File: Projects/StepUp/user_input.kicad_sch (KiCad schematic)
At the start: 3 parts

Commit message: feat(layout): Layout begins
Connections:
- net +3V3: now also JOY1.11 (1'); no longer JOY1.13 (3')
- net GND: now also JOY1.13 (3'); no longer JOY1.11 (1')
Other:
- note added: "Pins 1&2, resistance goes down as wiper moved in that direction E.g.: If joystick has pin 1 = 3v3 and pin 3 = GND, pin 2 voltage increases as josytick moved to pin 1, decreases as moved to pin 3"
- note added: "Wiper value"
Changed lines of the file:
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@@
+	)
+	(junction
+		(at 123.19 104.14)
+		(diameter 0)
+		(color 0 0 0 0)
 	)
 	(junction
@@
 		(color 0 0 0 0)
 	)
-	(junction
-		(at 123.19 99.06)
-		(diameter 0)
-		(color 0 0 0 0)
-	)
 	(no_connect
 		(at 158.75 104.14)
@@
 	(wire
 		(pts
+			(xy 123.19 104.14) (xy 128.27 104.14)
+		)
+		(stroke
+			(width 0)
+			(type default)
+		)
+	)
+	(wire
+		(pts
 			(xy 138.43 80.01) (xy 140.97 80.01)
 		)
@@
 	(wire
 		(pts
-			(xy 123.19 96.52) (xy 123.19 99.06)
+			(xy 123.19 96.52) (xy 123.19 104.14)
 		)
 		(stroke
@@
 	(wire
 		(pts
-			(xy 125.73 91.44) (xy 125.73 104.14)
-		)
-		(stroke
-			(width 0)
-			(type default)
-		)
-	)
-	(wire
-		(pts
 			(xy 125.73 80.01) (xy 125.73 77.47)
 		)
@@
 	(wire
 		(pts
+			(xy 125.73 99.06) (xy 128.27 99.06)
+		)
+		(stroke
+			(width 0)
+			(type default)
+		)
+	)
+	(wire
+		(pts
 			(xy 125.73 80.01) (xy 120.65 80.01)
 		)
@@
 	(wire
 		(pts
-			(xy 123.19 99.06) (xy 128.27 99.06)
-		)
-		(stroke
-			(width 0)
-			(type default)
-		)
-	)
-	(wire
-		(pts
 			(xy 168.91 91.44) (xy 168.91 118.11)
 		)
@@
 	(wire
 		(pts
+			(xy 125.73 91.44) (xy 125.73 99.06)
+		)
+		(stroke
+			(width 0)
+			(type default)
+		)
+	)
+	(wire
+		(pts
 			(xy 128.27 96.52) (xy 123.19 96.52)
 		)
@@
 	(wire
 		(pts
-			(xy 123.19 99.06) (xy 123.19 110.49)
-		)
-		(stroke
-			(width 0)
-			(type default)
-		)
-	)
-	(wire
-		(pts
-			(xy 125.73 104.14) (xy 128.27 104.14)
+			(xy 123.19 104.14) (xy 123.19 110.49)
 		)
 		(stroke
@@
 		(stroke
 			(width 0)
+			(type default)
+		)
+		(fill
+			(type none)
+		)
+	)
+	(rectangle
+		(start 156.845 69.85)
+		(end 233.045 83.82)
+		(stroke
+			(width 0.254)
 			(type default)
 		)
@@
 		)
 	)
+	(text "Wiper value"
+		(exclude_from_sim no)
+		(at 163.576 72.136 0)
+		(effects
+			(font
+				(size 1.27 1.27)
+				(bold yes)
+				(color 255 0 255 1)
+			)
+		)
+	)
+	(text "Pins 1&2, resistance goes down as wiper moved in that direction\nE.g.: If joystick has pin 1 = 3v3 and pin 3 = GND, pin 2 voltage\nincreases as josytick moved to pin 1, decreases as moved to pin 3"
+		(exclude_from_sim no)
+		(at 159.385 77.724 0)
+		(effects
+			(font
+				(size 1.27 1.27)
+			)
+			(justify left)
+		)
+	)

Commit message: feat(v0.2): Release, PCBs ordered!
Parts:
- JOY1: now in the parts list
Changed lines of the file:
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@@
 		(dnp no)
 		(fields_autoplaced yes)
-		(property "Reference" "#PWR097"
+		(property "Reference" "#PWR094"
 			(at 104.14 80.01 0)
 			(effects
@@
 			(project "StepUp"
 				(path "/e0cca1c7-c263-49eb-8c40-74000ebe5285/62dd6998-8b69-42c0-9c2f-b18953d44bc4"
-					(reference "#PWR097")
+					(reference "#PWR094")
 					(unit 1)
 				)
@@
 			)
 		)
+		(property "MANUFACTURER" ""
+			(at 134.62 80.01 0)
+			(effects
+				(font
+					(size 1.27 1.27)
+				)
+				(hide yes)
+			)
+		)
 		(pin "2"
 		)
@@
 		(unit 1)
 		(exclude_from_sim no)
-		(in_bom no)
+		(in_bom yes)
 		(on_board yes)
 		(dnp no)
@@
 		)
 		(property "SnapEDA_Link" ""
+			(at 128.27 91.44 0)
+			(effects
+				(font
+					(size 1.27 1.27)
+				)
+				(hide yes)
+			)
+		)
+		(property "MANUFACTURER" ""
 			(at 128.27 91.44 0)
 			(effects
@@
 		(dnp no)
 		(fields_autoplaced yes)
-		(property "Reference" "#PWR0101"
+		(property "Reference" "#PWR098"
 			(at 165.1 116.84 0)
 			(effects
@@
 			(project "StepUp"
 				(path "/e0cca1c7-c263-49eb-8c40-74000ebe5285/62dd6998-8b69-42c0-9c2f-b18953d44bc4"
-					(reference "#PWR0101")
+					(reference "#PWR098")
 					(unit 1)
 				)
@@
 		(dnp no)
 		(fields_autoplaced yes)
-		(property "Reference" "#PWR0100"
+		(property "Reference" "#PWR097"
 			(at 147.32 80.01 0)
 			(effects
@@
 			(project "StepUp"
 				(path "/e0cca1c7-c263-49eb-8c40-74000ebe5285/62dd6998-8b69-42c0-9c2f-b18953d44bc4"
-					(reference "#PWR0100")
+					(reference "#PWR097")
 					(unit 1)
 				)
@@
 			)
 		)
+		(property "MANUFACTURER" ""
+			(at 116.84 80.01 0)
+			(effects
+				(font
+					(size 1.27 1.27)
+				)
+				(hide yes)
+			)
+		)
 		(pin "2"
 		)
@@
 		(dnp no)
 		(fields_autoplaced yes)
-		(property "Reference" "#PWR098"
+		(property "Reference" "#PWR095"
 			(at 123.19 116.84 0)
 			(effects
@@
 			(project "StepUp"
 				(path "/e0cca1c7-c263-49eb-8c40-74000ebe5285/62dd6998-8b69-42c0-9c2f-b18953d44bc4"
-					(reference "#PWR098")
+					(reference "#PWR095")
 					(unit 1)
 				)
@@
 		(on_board yes)
 		(dnp no)
-		(property "Reference" "#PWR099"
+		(property "Reference" "#PWR096"
 			(at 125.73 81.28 0)
 			(effects
@@
 			(project "StepUp"
 				(path "/e0cca1c7-c263-49eb-8c40-74000ebe5285/62dd6998-8b69-42c0-9c2f-b18953d44bc4"
-					(reference "#PWR099")
+					(reference "#PWR096")
 					(unit 1)
 				)

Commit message: feat(v0.3): Begin work on next rev
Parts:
- renumbered C40 to C41, C41 to C42
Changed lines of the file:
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@@
 (kicad_sch
-	(version 20231120)
+	(version 20250114)
 	(generator "eeschema")
-	(generator_version "8.0")
+	(generator_version "9.0")
 	(paper "A4")
 	(title_block
 		(title "User Input")
-		(date "2024-04-28")
-		(rev "v0.2")
+		(date "2025-02-22")
+		(rev "v0.3")
 		(company "SJFOM")
+	)
+	(rectangle
+		(start 60.706 62.23)
+		(end 241.3 128.27)
+		(stroke
+			(width 0)
+			(type default)
+		)
+		(fill
+			(type none)
+		)
+	)
+	(rectangle
+		(start 156.845 69.85)
+		(end 233.045 83.82)
+		(stroke
+			(width 0.254)
+			(type default)
+		)
+		(fill
+			(type none)
+		)
+	)
+	(text "Wiper value"
+		(exclude_from_sim no)
+		(at 163.576 72.136 0)
+		(effects
+			(font
+				(size 1.27 1.27)
+				(bold yes)
+				(color 255 0 255 1)
+			)
+		)
+	)
+	(text "Pins 1&2, resistance goes down as wiper moved in that direction\nE.g.: If joystick has pin 1 = 3v3 and pin 3 = GND, pin 2 voltage\nincreases as josytick moved to pin 1, decreases as moved to pin 3"
+		(exclude_from_sim no)
+		(at 159.385 77.724 0)
+		(effects
+			(font
+				(size 1.27 1.27)
+			)
+			(justify left)
+		)
+	)
+	(text "Joystick"
+		(exclude_from_sim no)
+		(at 73.66 67.31 0)
+		(effects
+			(font
+				(face "KiCad Font")
+				(size 3.048 3.048)
+				(thickness 0.254)
+				(bold yes)
+				(color 29 232 255 1)
+			)
+		)
 	)
 	(junction
@@
 			(width 0)
 			(type default)
-		)
-	)
-	(rectangle
-		(start 60.706 62.23)
-		(end 241.3 128.27)
-		(stroke
-			(width 0)
-			(type default)
-		)
-		(fill
-			(type none)
-		)
-	)
-	(rectangle
-		(start 156.845 69.85)
-		(end 233.045 83.82)
-		(stroke
-			(width 0.254)
-			(type default)
-		)
-		(fill
-			(type none)
 		)
 	)
@@
 			"RERERAwMiIiIiIiIgQEREREREdkxMCAiIiIiIgYGRERERETEwICIiIiIiOwYGBAREREREQMDIiIi"
 			"IiJiYEBERERERHYMDIiIiIiIiIEBERERERExMCAiIiIiIhH5P6/Y9CjKHXtVAAAAAElFTkSuQmCC"
-		)
-	)
-	(text "Wiper value"
-		(exclude_from_sim no)
-		(at 163.576 72.136 0)
-		(effects
-			(font
-				(size 1.27 1.27)
-				(bold yes)
-				(color 255 0 255 1)
-			)
-		)
-	)
-	(text "Pins 1&2, resistance goes down as wiper moved in that direction\nE.g.: If joystick has pin 1 = 3v3 and pin 3 = GND, pin 2 voltage\nincreases as josytick moved to pin 1, decreases as moved to pin 3"
-		(exclude_from_sim no)
-		(at 159.385 77.724 0)
-		(effects
-			(font
-				(size 1.27 1.27)
-			)
-			(justify left)
-		)
-	)
-	(text "Joystick"
-		(exclude_from_sim no)
-		(at 73.66 67.31 0)
-		(effects
-			(font
-				(face "KiCad Font")
-				(size 3.048 3.048)
-				(thickness 0.254)
-				(bold yes)
-				(color 29 232 255 1)
-			)
+			"AAAAAAAAAAAAAAAAAAAAAAAAAAAAAAAAAAAAAAAAAAAAAAAAAAAAAAAAAAAAAAAAAAAAAAAAAAAA"
+			"AAAAAAAAAAAAAAAAAAAAAAAAAAAAAAAAAAAAAAAAAAAAAAAAAAAAAAAAAAAAAAAAAAAAAAAAAAAA"
+			"AAAAAAAAAAAAAAAAAAAAAAAAAAAAAAAAAAAAAAAAAAAAAAAAAAAAAAAAAAAAAAAAAAAAAAAAAAAA"
+			"AAAAAAAAAAAAAAAAAAAAAAAAAAAAAAAAAAAAAAAAAAAAAAAAAAAAAAAAAAAAAAAAAAAAAAAAAAAA"
+			"AAAAAAAAAAAAAAAAAAAAAAAAAAAAAAAAAAAAAAAAAAAAAAAAAAAAAAAAAAAAAAAAAAAAAAAAAAAA"
+			"AAAAAAAAAAAAAAAAAAAAAAAAAAAAAAAAAAAAAAAAAAAAAAAAAAAAAAAAAAAAAAAAAAAAAAAAAAAA"
+			"AAAAAAAAAAAAAAAAAAAAAAAAAAAAAAAAAAAAAAAAAAAAAAAAAAAAAAAAAAAAAAAAAAAAAAAAAAAA"
+			"AAAAAAAAAAAAAAAAAAAAAAAAAAAAAAAAAAAAAAAAAAAAAAAAAAAAAAAAAAAAAAAAAAAAAAAAAAAA"
+			"AAAAAAAAAAAAAAAAAAAAAAAAAAAAAAAAAAAAAAAAAAAAAAAAAAAAAAAAAAAAAAAAAAAAAAAAAAAA"
+			"AAAAAAAAAAAAAAAAAAAAAAAAAAAAAAAAAAAAAAAAAAAAAAAAAAAAAAAAAAAAAAAAAAAAAAAAAAAA"
+			"AAAAAAAAAAAAAAAAAAAAAAAAAAAAAAAAAAAAAAAAAAAAAAAAAAAAAAAAAAAAAAAAAAAAAAAAAAAA"
+			"AAAAAAAAAAAAAAAAAAAAAAAAAAAAAAAAAAAAAAAAAAAAAAAAAAAAAAAAAAAAAAAAAAAAAAAAAAAA"
+			"AAAAAAAAAAAAAAAAAAAAAAAAAAAAAAAAAAAAAAAAAAAAAAAAAAAAAAAAAAAAAAAAAAAAAAAAAAAA"
+			"AAAAAAAAAAAAAAAAAAAAAAAAAAAAAAAAAAAAAAAAAAAAAAAAAAAAAAAAAAAAAAAAAAAAAAAAAAAA"
+			"AAAAAAAAAAAAAAAAAAAAAAAAAAAAAAAAAAAAAAAAAAAAAAAAAAAAAAAAAAAAAAAAAAAAAAAAAAAA"
+			"AAAAAAAAAAAAAAAAAAAAAAAAAAAAAAAAAAAAAAAAAAAAAAAAAAAAAAAAAAAAAAAAAAAAAAAAAAAA"
+			"AAAAAAAAAAAAAAAAAAAAAAAAAAAAAAAAAAAAAAAAAAAAAAAAAAAAAAAAAAAAAAAAAAAAAAAAAAAA"
+			"AAAAAAAAAAAAAAAAAAAAAAAAAAAAAAAAAAAAAAAAAAAAAAAAAAAAAAAAAAAAAAAAAAAAAAAAAAAA"
+			"AAAAAAAAAAAAAAAAAAAAAAAAAAAAAAAAAAAAAAAAAAAAAAAAAAAAAAAAAAAAAAAAAAAAAAAAAAAA"
+			"AAAAAAAAAAAAAAAAAAAAAAAAAAAAAAAAAAAAAAAAAAAAAAAAAAAAAAAAAAAAAAAAAAAAAAAAAAAA"
+			"AAAAAAAAAAAAAAAAAAAAAAAAAAAAAAAAAAAAAAAAAAAAAAAAAAAAAAAAAAAAAAAAAAAAAAAAAAAA"
+			"AAAAAAAAAAAAAAAAAAAAAAAAAAAAAAAAAAAAAAAAAAAAAAAAAAAAAAAAAAAAAAAAAAAAAAAAAAAA"
+			"AAAAAAAAAAAAAAAAAAAAAAAAAAAAAAAAAAAAAAAAAAAAAAAAAAAAAAAAAAAAAAAAAAAAAAAAAAAA"
+			"AAAAAAAAAAAAAAAAAAAAAAAAAAAAAAAAAAAAAAAAAAAAAAAAAAAAAAAAAAAAAAAAAAAAAAAAAAAA"
+			"AAAAAAAAAAAAAAAAAAAAAAAAAAAAAAAAAAAAAAAAAAAAAAAAAAAAAAAAAAAAAAAAAAAAAAAAAAAA"
+			"AAAAAAAAAAAAAAAAAAAAAAAAAAAAAAAAAAAAAAAAAAAAAAAAAAAAAAAAAAAAAAAAAAAAAAAAAAAA"
+			"AAAAAAAAAAAAAAAAAAAAAAAAAAAAAAAAAAAAAAAAAAAAAAAAAAAAAAAAAAAAAAAAAAAAAAAAAAAA"
+			"AAAAAAAAAAAAAAAAAAAAAAAAAAAAAAAAAAAAAAAAAAAAAAAAAAAAAAAAAAAAAAAAAAAAAAAAAAAA"
+			"AAAAAAAAAAAAAAAAAAAAAAAAAAAAAAAAAAAAAAAAAAAAAAAAAAAAAAAAAAAAAAAAAAAAAAAAAAAA"
+			"AAAAAAAAAAAAAAAAAAAAAAAAAAAAAAAAAAAAAAAAAAAAAAAABAAAAHxaWADwAF66UQIAAPAAXrpR"
+			"AgAAYADB1FECAABgAMHUUQIAAAAgGNVRAgAAANClAAAAAAAAAAAAAAAAAAAAAAAAAAAAAAAAAAAA"
+			"AAAAAAAAAAAAAAAAAAAAAAAAAAAAAAAAAAAAAAAAAAAAAAAAAAAAAAAAAAAAAAAAAAAAAAAAAAAA"
+			"AAAAAAAAAAAAAAAAAAAAAAAAAAAAAAAAAAAAAAAAAAAAAAAAAAAAAAAAAAAAAAAAAAAAAAAAAAAA"
+			"AAAAAAAAAAAAAAAAAAAAAAAAAAAAAAAAAAAAAAAAAAAAAAAAAAAAAAAAAAAAAAAAAAAAAAAAAAAA"
+			"AAAAAAAAAAAAAAAAAAAAAAAAAAAAAAAAAAAAAAAAAAAAAAAAAAAAAAAAAAAAAAAAAAAAAAAAAAAA"
+			"AAAAAAAAAAAAAAAAAAAAAAAAAAAAAAAAAAAAAAAAAAAAAAAAAAAAAAAAAAAAAAAAAAAAAAAAAAAA"
+			"AAAAAAAAAAAAAAAAAAAAAAAAAAAAAAAAAAAAAAAAAAAAAAAAAAAAAAAAAAAAAAAAAAAAAAAAAAAA"
+			"AAAAAAAAAAAAAAAAAAAAAAAAAAAAAAAAAAAAAAAAAAAAAAAAAAAAAAAAAAAAAAAAAAAAAAAAAAAA"
+			"AAAAAAAAAAAAAAAAAAAAAAAAAAAAAAAAAAAAAAAAAAAAAAAAAAAAAAAAAAAAAAAAAAAAAAAAAAAA"
+			"AAAAAAAAAAAAAAAAAAAAAAAAAAAAAAAAAAAAAAAAAAAAAAAAAAAAAAAAAAAAAAAAAAAAAAAAAAAA"
+			"AAAAAAAAAAAAAAAAAAAAAAAAAAAAAAAAAAAAAAAAAAAAAAAAAAAAAAAAAAAAAAAAAAAAAAAAAAAA"
+			"AAAAAAAAAAAAAAAAAAAAAAAAAAAAAAAAAAAAAAAAAAAAAAAAAAAAAAAAAAAAAAAAAAAAAAAAAAAA"
+			"AAAAAAAAAAAAAAAAAAAAAAAAAAAAAAAAAAAAAAAAAAAAAAAAAAAAAAAAAAAAAAAAAAAAAAAAAAAA"
+			"AAAAAAAAAAAAAAAAAAAAAAAAAAAAAAAAAAAAAAAAAAAAAAAAAAAAAAAAAAAAAAAAAAAAAAAAAAAA"
+			"AAAAAAAAAAAAAAAAAAAAAAAAAAAAAAAAAAAAAAAAAAAAAAAAAAAAAAAAAAAAAAAAAAAAAAAAAAAA"
+			"AAAAAAAAAAAAAAAAAAAAAAAAAAAAAAAAAAAAAAAAAAAAAAAAAAAAAAAAAAAAAAAAAAAAAAAAAAAA"
+			"AAAAAAAAAAAAAAAAAAAAAAAAAAAAAAAAAAAAAAAAAAAAAAAAAAAAAAAAAAAAAAAAAAAAAAAAAAAA"
+			"AAAAAAAAAAAAAAAAAAAAAAAAAAAAAAAAAAAAAAAAAAAAAAAAAAAAAAAAAAAAAAAAAAAAAAAAAAAA"
+			"AAAAAAAAAAAAAAAAAAAAAAAAAAAAAAAAAAAAAAAAAAAAAAAAAAAAAAAAAAAAAAAAAAAAAAAAAAAA"
+			"AAAAAAAAAAAAAAAAAAAAAAAAAAAAAAAAAAAAAAAAAAAAAAAAAAAAAAAAAAAAAAAAAAAAAAAAAAAA"
+			"AAAAAAAAAAAAAAAAAAAAAAAAAAAAAAAAAAAAAAAAAAAAAAAAAAAAAAAAAAAAAAAAAAAAAAAAAAAA"
+			"AAAAAAAAAAAAAAAAAAAAAAAAAAAAAAAAAAAAAAAAAAAAAAAAAAAAAAAAAAAAAAAAAAAAAAAAAAAA"
+			"AAAAAAAAAAAAAAAAAAAAAAAAAAAAAAAAAAAAAAAAAAAAAAAAAAAAAAAAAAAAAAAAAAAAAAAAAAAA"
+			"AAAAAAAAAAAAAAAAAAAAAAAAAAAAAAAAAAAAAAAAAAAAAAAAAAAAAAAAAAAAAAAAAAAAAAAAAA=="
 		)
 	)
@@
 		(dnp no)
 		(fields_autoplaced yes)
-		(property "Reference" "#PWR094"
+		(property "Reference" "#PWR099"
 			(at 104.14 80.01 0)
 			(effects
@@
 			(project "StepUp"
 				(path "/e0cca1c7-c263-49eb-8c40-74000ebe5285/62dd6998-8b69-42c0-9c2f-b18953d44bc4"
-					(reference "#PWR094")
+					(reference "#PWR099")
 					(unit 1)
 				)
@@
 		(on_board yes)
 		(dnp no)
-		(property "Reference" "C41"
+		(property "Reference" "C42"
 			(at 132.08 78.232 90)
 			(effects
@@
 			(project "StepUp"
 				(path "/e0cca1c7-c263-49eb-8c40-74000ebe5285/62dd6998-8b69-42c0-9c2f-b18953d44bc4"
-					(reference "C41")
+					(reference "C42")
 					(unit 1)
 				)
@@
 		(dnp no)
 		(fields_autoplaced yes)
-		(property "Reference" "#PWR098"
+		(property "Reference" "#PWR0103"
 			(at 165.1 116.84 0)
 			(effects
@@
 			(project "StepUp"
 				(path "/e0cca1c7-c263-49eb-8c40-74000ebe5285/62dd6998-8b69-42c0-9c2f-b18953d44bc4"
-					(reference "#PWR098")
+					(reference "#PWR0103")
 					(unit 1)
 				)
@@
 		(dnp no)
 		(fields_autoplaced yes)
-		(property "Reference" "#PWR097"
+		(property "Reference" "#PWR0102"
 			(at 147.32 80.01 0)
 			(effects
@@
 			(project "StepUp"
 				(path "/e0cca1c7-c263-49eb-8c40-74000ebe5285/62dd6998-8b69-42c0-9c2f-b18953d44bc4"
-					(reference "#PWR097")
+					(reference "#PWR0102")
 					(unit 1)
 				)
@@
 		(on_board yes)
 		(dnp no)
-		(property "Reference" "C40"
+		(property "Reference" "C41"
 			(at 119.38 81.788 90)
 			(effects
@@
 			(project "StepUp"
 				(path "/e0cca1c7-c263-49eb-8c40-74000ebe5285/62dd6998-8b69-42c0-9c2f-b18953d44bc4"
-					(reference "C40")
+					(reference "C41")
 					(unit 1)
 				)
@@
 		(dnp no)
 		(fields_autoplaced yes)
-		(property "Reference" "#PWR095"
+		(property "Reference" "#PWR0100"
 			(at 123.19 116.84 0)
 			(effects
@@
 			(project "StepUp"
 				(path "/e0cca1c7-c263-49eb-8c40-74000ebe5285/62dd6998-8b69-42c0-9c2f-b18953d44bc4"
-					(reference "#PWR095")
+					(reference "#PWR0100")
 					(unit 1)
 				)
@@
 		(on_board yes)
 		(dnp no)
-		(property "Reference" "#PWR096"
+		(property "Reference" "#PWR0101"
 			(at 125.73 81.28 0)
 			(effects
@@
 			(project "StepUp"
 				(path "/e0cca1c7-c263-49eb-8c40-74000ebe5285/62dd6998-8b69-42c0-9c2f-b18953d44bc4"
-					(reference "#PWR096")
+					(reference "#PWR0101")
 					(unit 1)
 				)

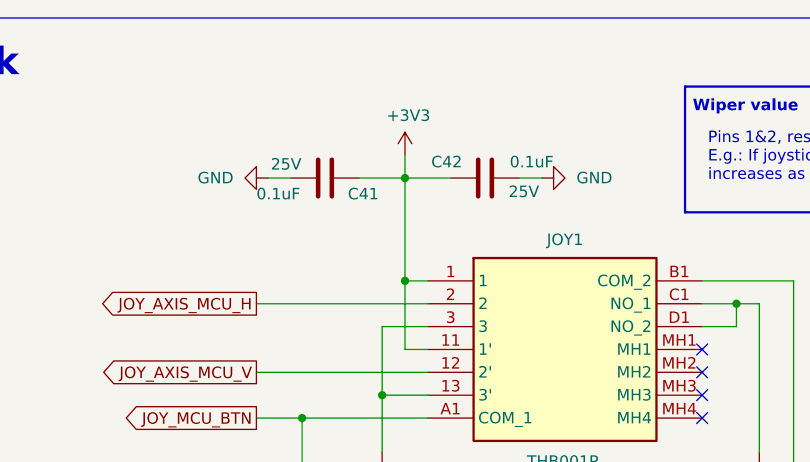
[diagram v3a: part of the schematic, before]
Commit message: feat(v0.3): Boost layout complete
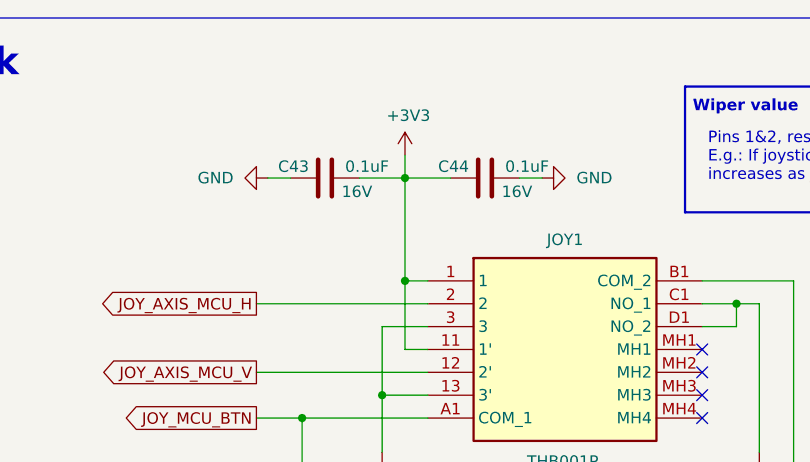
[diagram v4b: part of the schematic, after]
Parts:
- removed C41, C42: 0.1uF, Capacitor_SMD:C_0603_1608Metric, symbol Device:C
- added C43, C44: 0.1uF, Capacitor_SMD:C_0402_1005Metric, symbol Device:C
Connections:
- net +3V3: now also C43.2, C44.1
- net GND: now also C43.1, C44.2
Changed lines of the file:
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@@
+			"AAAAAAAAAAAAAAAAAAAAAAAAAAAAAAAAAAAAAAAAAAAAAAAAAAAAAAAAAAAAAAAAAAAAAAAAAAAA"
+			"AAAAAAAAAAAAAAAAAAAAAAAAAAAAAAAAAAAAAAAAAAAAAAAAAAAAAAAAAAAAAAAAAAAAAAAAAAAA"
+			"AAAAAAAAAAAAAAAAAAAAAAAAAAAAAAAAAAAAAAAAAAAAAAAAAAAAAAAAAAAAAAAAAAAAAAAAAAAA"
+			"AAAAAAAAAAAAAAAAAAAAAAAAAAAAAAAAAAAAAAAAAAAAAAAAAAAAAAAAAAAAAAAAAAAAAAAAAAAA"
+			"AAAAAAAAAAAAAAAAAAAAAAAAAAAAAAAAAAAAAAAAAAAAAAAAAAAAAAAAAAAAAAAAAAAAAAAAAAAA"
+			"AAAAAAAAAAAAAAAAAAAAAAAAAAAAAAAAAAAAAAAAAAAAAAAAAAAAAAAAAAAAAAAAAAAAAAAAAAAA"
+			"AAAAAAAAAAAAAAAAAAAAAAAAAAAAAAAAAAAAAAAAAAAAAAAAAAAAAAAAAAAAAAAAAAAAAAAAAAAA"
+			"AAAAAAAAAAAAAAAAAAAAAAAAAAAAAAAAAAAAAAAAAAAAAAAAAAAAAAAAAAAAAAAAAAAAAAAAAAAA"
+			"AAAAAAAAAAAAAAAAAAAAAAAAAAAAAAAAAAAAAAAAAAAAAAAAAAAAAAAAAAAAAAAAAAAAAAAAAAAA"
+			"AAAAAAAAAAAAAAAAAAAAAAAAAAAAAAAAAAAAAAAAAAAAAAAAAAAAAAAAAAAAAAAAAAAAAAAAAAAA"
+			"AAAAAAAAAAAAAAAAAAAAAAAAAAAAAAAAAAAAAAAAAAAAAAAAAAAAAAAAAAAAAAAAAAAAAAAAAAAA"
+			"AAAAAAAAAAAAAAAAAAAAAAAAAAAAAAAAAAAAAAAAAAAAAAAAAAAAAAAAAAAAAAAAAAAAAAAAAAAA"
+			"AAAAAAAAAAAAAAAAAAAAAAAAAAAAAAAAAAAAAAAAAAAAAAAAAAAAAAAAAAAAAAAAAAAAAAAAAAAA"
+			"AAAAAAAAAAAAAAAAAAAAAAAAAAAAAAAAAAAAAAAAAAAAAAAAAAAAAAAAAAAAAAAAAAAAAAAAAAAA"
+			"AAAAAAAAAAAAAAAAAAAAAAAAAAAAAAAAAAAAAAAAAAAAAAAAAAAAAAAAAAAAAAAAAAAAAAAAAAAA"
+			"AAAAAAAAAAAAAAAAAAAAAAAAAAAAAAAAAAAAAAAAAAAAAAAAAAAAAAAAAAAAAAAAAAAAAAAAAAAA"
+			"AAAAAAAAAAAAAAAAAAAAAAAAAAAAAAAAAAAAAAAAAAAAAAAAAAAAAAAAAAAAAAAAAAAAAAAAAAAA"
+			"AAAAAAAAAAAAAAAAAAAAAAAAAAAAAAAAAAAAAAAAAAAAAAAAAAAAAAAAAAAAAAAAAAAAAAAAAAAA"
 			"AAAAAAAAAAAAAAAAAAAAAAAAAAAAAAAAAAAAAAAAAAAAAAAAAAAAAAAAAAAAAAAAAAAAAAAAAAAA"
 			"AAAAAAAAAAAAAAAAAAAAAAAAAAAAAAAAAAAAAAAAAAAAAAAAAAAAAAAAAAAAAAAAAAAAAAAAAAAA"
@@
 		(on_board yes)
 		(dnp no)
-		(property "Reference" "C42"
-			(at 132.08 78.232 90)
+		(property "Reference" "C44"
+			(at 132.842 78.74 90)
 			(effects
 				(font
@@
 		)
 		(property "Value" "0.1uF"
-			(at 142.24 78.232 90)
+			(at 141.732 78.74 90)
 			(effects
 				(font
@@
 			)
 		)
-		(property "Footprint" "Capacitor_SMD:C_0603_1608Metric"
+		(property "Footprint" "Capacitor_SMD:C_0402_1005Metric"
 			(at 138.43 79.0448 0)
 			(effects
@@
 			)
 		)
-		(property "Voltage" "25V"
-			(at 138.938 81.534 90)
+		(property "Voltage" "16V"
+			(at 138.176 81.534 90)
 			(effects
 				(font
@@
 			)
 		)
-		(property "Package" "0603"
-			(at 134.62 80.01 0)
-			(effects
-				(font
-					(size 1.27 1.27)
-				)
-				(hide yes)
-			)
-		)
-		(property "Dielectric" "X7R"
-			(at 134.62 80.01 0)
-			(effects
-				(font
-					(size 1.27 1.27)
-				)
-				(hide yes)
-			)
-		)
-		(property "MPN" "CC0603KRX7R8BB104"
-			(at 134.62 80.01 0)
-			(effects
-				(font
-					(size 1.27 1.27)
-				)
-				(hide yes)
-			)
-		)
-		(property "Manufacturer" "YAGEO"
+		(property "Package" "0402"
+			(at 134.62 80.01 0)
+			(effects
+				(font
+					(size 1.27 1.27)
+				)
+				(hide yes)
+			)
+		)
+		(property "Dielectric" "X5R"
+			(at 134.62 80.01 0)
+			(effects
+				(font
+					(size 1.27 1.27)
+				)
+				(hide yes)
+			)
+		)
+		(property "MPN" "GRM155R61C104KA88D"
+			(at 134.62 80.01 0)
+			(effects
+				(font
+					(size 1.27 1.27)
+				)
+				(hide yes)
+			)
+		)
+		(property "Manufacturer" "Murata"
 			(at 134.62 80.01 0)
 			(effects
@@
 			(project "StepUp"
 				(path "/e0cca1c7-c263-49eb-8c40-74000ebe5285/62dd6998-8b69-42c0-9c2f-b18953d44bc4"
-					(reference "C42")
+					(reference "C44")
 					(unit 1)
 				)
@@
 	(symbol
 		(lib_id "Device:C")
-		(at 116.84 80.01 270)
+		(at 116.84 80.01 90)
 		(unit 1)
 		(exclude_from_sim no)
@@
 		(on_board yes)
 		(dnp no)
-		(property "Reference" "C41"
-			(at 119.38 81.788 90)
+		(property "Reference" "C43"
+			(at 115.062 78.74 90)
 			(effects
 				(font
@@
 		)
 		(property "Value" "0.1uF"
-			(at 109.22 81.788 90)
+			(at 123.952 78.74 90)
 			(effects
 				(font
@@
 			)
 		)
-		(property "Footprint" "Capacitor_SMD:C_0603_1608Metric"
-			(at 113.03 80.9752 0)
+		(property "Footprint" "Capacitor_SMD:C_0402_1005Metric"
+			(at 120.65 79.0448 0)
 			(effects
 				(font
@@
 			)
 		)
-		(property "Voltage" "25V"
-			(at 112.522 78.486 90)
+		(property "Voltage" "16V"
+			(at 120.396 81.534 90)
 			(effects
 				(font
@@
 			)
 		)
-		(property "Package" "0603"
-			(at 116.84 80.01 0)
-			(effects
-				(font
-					(size 1.27 1.27)
-				)
-				(hide yes)
-			)
-		)
-		(property "Dielectric" "X7R"
-			(at 116.84 80.01 0)
-			(effects
-				(font
-					(size 1.27 1.27)
-				)
-				(hide yes)
-			)
-		)
-		(property "MPN" "CC0603KRX7R8BB104"
-			(at 116.84 80.01 0)
-			(effects
-				(font
-					(size 1.27 1.27)
-				)
-				(hide yes)
-			)
-		)
-		(property "Manufacturer" "YAGEO"
+		(property "Package" "0402"
+			(at 116.84 80.01 0)
+			(effects
+				(font
+					(size 1.27 1.27)
+				)
+				(hide yes)
+			)
+		)
+		(property "Dielectric" "X5R"
+			(at 116.84 80.01 0)
+			(effects
+				(font
+					(size 1.27 1.27)
+				)
+				(hide yes)
+			)
+		)
+		(property "MPN" "GRM155R61C104KA88D"
+			(at 116.84 80.01 0)
+			(effects
+				(font
+					(size 1.27 1.27)
+				)
+				(hide yes)
+			)
+		)
+		(property "Manufacturer" "Murata"
 			(at 116.84 80.01 0)
 			(effects
@@
 			(project "StepUp"
 				(path "/e0cca1c7-c263-49eb-8c40-74000ebe5285/62dd6998-8b69-42c0-9c2f-b18953d44bc4"
-					(reference "C41")
+					(reference "C43")
 					(unit 1)
 				)
